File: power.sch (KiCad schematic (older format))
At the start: 7 parts, among them U2 LM2776, U3 LT1761-5

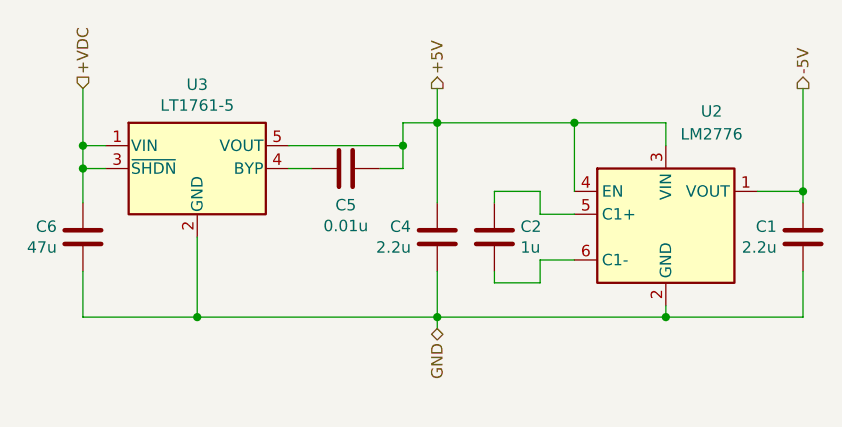
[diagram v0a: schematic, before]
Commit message: Align power wires cosmetically
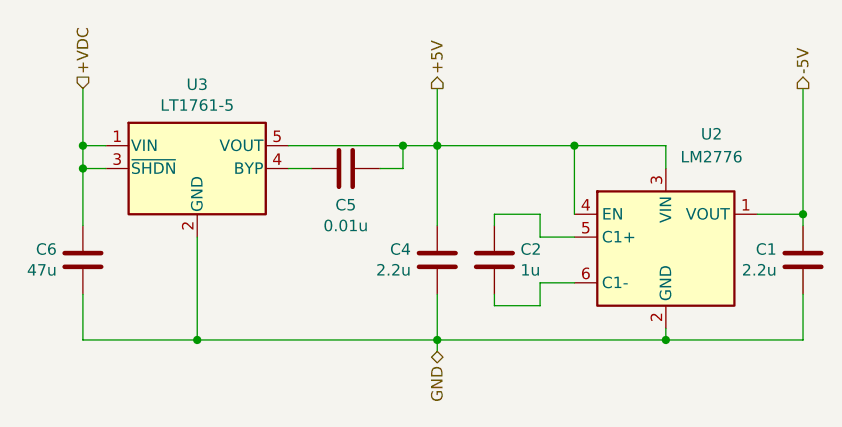
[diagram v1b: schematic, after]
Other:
- moved on the sheet: C1, C2, C4, C6, U2
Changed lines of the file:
@@
 Comment4 ""
 $EndDescr
-Wire Wire Line
-	5650 3500 5650 3600
 $Comp
 L Device:C C?
 U 1 1 5ECE4C57
-P 4250 4000
+P 4250 4100
 AR Path="/5ECE4C57" Ref="C?"  Part="1"
 AR Path="/5ECDCFC2/5ECE4C57" Ref="C6"  Part="1"
-F 0 "C6" H 4136 4046 50  0000 R CNN
-F 1 "47u" H 4136 3955 50  0000 R CNN
-F 2 "Capacitor_SMD:C_1206_3216Metric" H 4288 3850 50  0001 C CNN
-F 3 "https://octopart.com/c3216x5r1e476m160ac-tdk-25947783?r=sp" H 4250 4000 50  0001 C CNN
-	1    4250 4000
+F 0 "C6" H 4136 4146 50  0000 R CNN
+F 1 "47u" H 4136 4055 50  0000 R CNN
+F 2 "Capacitor_SMD:C_1206_3216Metric" H 4288 3950 50  0001 C CNN
+F 3 "https://octopart.com/c3216x5r1e476m160ac-tdk-25947783?r=sp" H 4250 4100 50  0001 C CNN
+	1    4250 4100
 	1    0    0    -1
 $EndComp
@@
 L Regulator_SwitchedCapacitor:LM2776 U?
 U 1 1 5ECE4C7F
-P 6800 3900
+P 6800 4000
 AR Path="/5ECE4C7F" Ref="U?"  Part="1"
 AR Path="/5ECDCFC2/5ECE4C7F" Ref="U2"  Part="1"
-F 0 "U2" H 7000 4350 50  0000 C CNN
-F 1 "LM2776" H 7000 4250 50  0000 C CNN
-F 2 "Package_TO_SOT_SMD:SOT-23-6" H 6850 3550 50  0001 L CNN
-F 3 "http://www.ti.com/lit/ds/symlink/lm2776.pdf" H 4950 5150 50  0001 C CNN
-	1    6800 3900
+F 0 "U2" H 7000 4450 50  0000 C CNN
+F 1 "LM2776" H 7000 4350 50  0000 C CNN
+F 2 "Package_TO_SOT_SMD:SOT-23-6" H 6850 3650 50  0001 L CNN
+F 3 "http://www.ti.com/lit/ds/symlink/lm2776.pdf" H 4950 5250 50  0001 C CNN
+	1    6800 4000
 	1    0    0    -1
 $EndComp
 Wire Wire Line
-	5800 4150 5800 4350
+	5800 4250 5800 4450
 Wire Wire Line
-	7400 4150 7400 4350
+	7400 4250 7400 4450
 $Comp
 L Device:C C?
 U 1 1 5ECE4C89
-P 6050 4000
+P 6050 4100
 AR Path="/5ECE4C89" Ref="C?"  Part="1"
 AR Path="/5ECDCFC2/5ECE4C89" Ref="C2"  Part="1"
-F 0 "C2" H 5936 4046 50  0000 R CNN
-F 1 "1u" H 5936 3955 50  0000 R CNN
-F 2 "Capacitor_SMD:C_0603_1608Metric" H 6088 3850 50  0001 C CNN
-F 3 "~" H 6050 4000 50  0001 C CNN
-	1    6050 4000
+F 0 "C2" H 5936 4146 50  0000 R CNN
+F 1 "1u" H 5936 4055 50  0000 R CNN
+F 2 "Capacitor_SMD:C_0603_1608Metric" H 6088 3950 50  0001 C CNN
+F 3 "~" H 6050 4100 50  0001 C CNN
+	1    6050 4100
 	-1   0    0    -1
 $EndComp
 Wire Wire Line
-	7400 3800 7400 3850
+	7400 3900 7400 3950
 Wire Wire Line
-	7200 3800 7400 3800
-Connection ~ 7400 3800
+	7200 3900 7400 3900
+Connection ~ 7400 3900
 Wire Wire Line
-	7400 3350 7400 3800
+	7400 3350 7400 3900
 $Comp
 L Device:C C?
 U 1 1 5ECE4C95
-P 7400 4000
+P 7400 4100
 AR Path="/5ECE4C95" Ref="C?"  Part="1"
 AR Path="/5ECDCFC2/5ECE4C95" Ref="C1"  Part="1"
-F 0 "C1" H 7285 3954 50  0000 R CNN
-F 1 "2.2u" H 7285 4045 50  0000 R CNN
-F 2 "Capacitor_SMD:C_0603_1608Metric" H 7438 3850 50  0001 C CNN
-F 3 "~" H 7400 4000 50  0001 C CNN
-	1    7400 4000
+F 0 "C1" H 7285 4054 50  0000 R CNN
+F 1 "2.2u" H 7285 4145 50  0000 R CNN
+F 2 "Capacitor_SMD:C_0603_1608Metric" H 7438 3950 50  0001 C CNN
+F 3 "~" H 7400 4100 50  0001 C CNN
+	1    7400 4100
 	1    0    0    1
 $EndComp
 Wire Wire Line
-	7400 4350 6800 4350
+	7400 4450 6800 4450
 Wire Wire Line
-	6800 4350 5800 4350
-Connection ~ 6800 4350
+	6800 4450 5800 4450
+Connection ~ 6800 4450
 Wire Wire Line
-	6800 4350 6800 4300
+	6800 4450 6800 4400
 Wire Wire Line
-	6050 4200 6050 4150
+	6050 4300 6050 4250
 Wire Wire Line
-	6250 4200 6050 4200
+	6250 4300 6050 4300
 Wire Wire Line
-	6250 4100 6250 4200
+	6250 4200 6250 4300
 Wire Wire Line
-	6400 4100 6250 4100
+	6400 4200 6250 4200
 Wire Wire Line
-	6050 3800 6050 3850
+	6050 3900 6050 3950
 Wire Wire Line
-	6250 3800 6050 3800
+	6250 3900 6050 3900
 Wire Wire Line
-	6250 3900 6250 3800
+	6250 4000 6250 3900
 Wire Wire Line
-	6400 3900 6250 3900
+	6400 4000 6250 4000
 Wire Wire Line
-	6400 3800 6400 3500
+	6400 3900 6400 3600
 Wire Wire Line
-	6800 3500 6800 3600
+	6800 3600 6800 3700
 Wire Wire Line
-	5800 3850 5800 3500
+	5800 3950 5800 3600
 Wire Wire Line
-	5650 3500 5800 3500
+	6400 3600 5800 3600
+Connection ~ 5800 3600
+Connection ~ 6400 3600
 Wire Wire Line
-	6400 3500 5800 3500
-Connection ~ 5800 3500
-Connection ~ 6400 3500
+	6800 3600 6400 3600
+Connection ~ 5800 4450
 Wire Wire Line
-	6800 3500 6400 3500
-Connection ~ 5800 4350
-Wire Wire Line
-	5800 4350 5800 4400
+	5800 4450 5800 4500
 Text HLabel 7400 3350 1    50   Output ~ 0
 -5V
@@
 +5V
 Wire Wire Line
-	5800 3500 5800 3350
+	5800 3600 5800 3350
 Wire Wire Line
-	4750 4000 4750 4350
+	4750 4000 4750 4450
 Wire Wire Line
-	4750 4350 5800 4350
-Text HLabel 5800 4400 3    50   BiDi ~ 0
+	4750 4450 5800 4450
+Text HLabel 5800 4500 3    50   BiDi ~ 0
 GND
 Text HLabel 4250 3350 1    50   Input ~ 0
 +VDC
 Wire Wire Line
-	4750 4350 4250 4350
+	4750 4450 4250 4450
 Wire Wire Line
-	4250 4350 4250 4150
-Connection ~ 4750 4350
+	4250 4450 4250 4250
+Connection ~ 4750 4450
 Wire Wire Line
-	4250 3850 4250 3700
+	4250 3950 4250 3700
 Wire Wire Line
 	5650 3600 5150 3600
@@
 L Device:C C?
 U 1 1 5ECE4CB8
-P 5800 4000
+P 5800 4100
 AR Path="/5ECE4CB8" Ref="C?"  Part="1"
 AR Path="/5ECDCFC2/5ECE4CB8" Ref="C4"  Part="1"
-F 0 "C4" H 5685 3954 50  0000 R CNN
-F 1 "2.2u" H 5685 4045 50  0000 R CNN
-F 2 "Capacitor_SMD:C_0603_1608Metric" H 5838 3850 50  0001 C CNN
-F 3 "~" H 5800 4000 50  0001 C CNN
-	1    5800 4000
+F 0 "C4" H 5685 4054 50  0000 R CNN
+F 1 "2.2u" H 5685 4145 50  0000 R CNN
+F 2 "Capacitor_SMD:C_0603_1608Metric" H 5838 3950 50  0001 C CNN
+F 3 "~" H 5800 4100 50  0001 C CNN
+	1    5800 4100
 	1    0    0    1
 $EndComp
@@
 Wire Wire Line
 	5650 3700 5650 3600
+Wire Wire Line
+	5650 3600 5800 3600
 Connection ~ 5650 3600
 $EndSCHEMATC
